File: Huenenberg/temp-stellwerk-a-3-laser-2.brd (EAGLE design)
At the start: 99.1 x 61 mm, 120 parts, among them Q1 BSS123, Q10 BSS84, Q11 BSS123, Q12 BSS84, Q13 BSS123, Q14 BSS84, Q15 BSS123, Q16 BSS84, Q17 BSS123, Q18 BSS84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

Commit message: Adds circles to laser around the tactile buttons.
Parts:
- H1, H2, H3: value MOUNT-HOLE3.2 -> MOUNT-HOLE4.0-LASER; device holes:3,2 -> eagleparts:MOUNT-HOLE-3.2-4.0-LASER
- LOCK, W1, W1011, W34, W56, W89: device g-e2e-training:TACTSW-6X6 -> eagleparts:TACTSW-6X6-LASER
- TRK1, TRK2, TRK3, TRK4, TRK5, TRK6, W2A, W2B, W7A, W7B: value (none) -> TACTSW-6X6S; device g-e2e-training:TACTSW-6X6 -> eagleparts:TACTSW-6X6-LASER

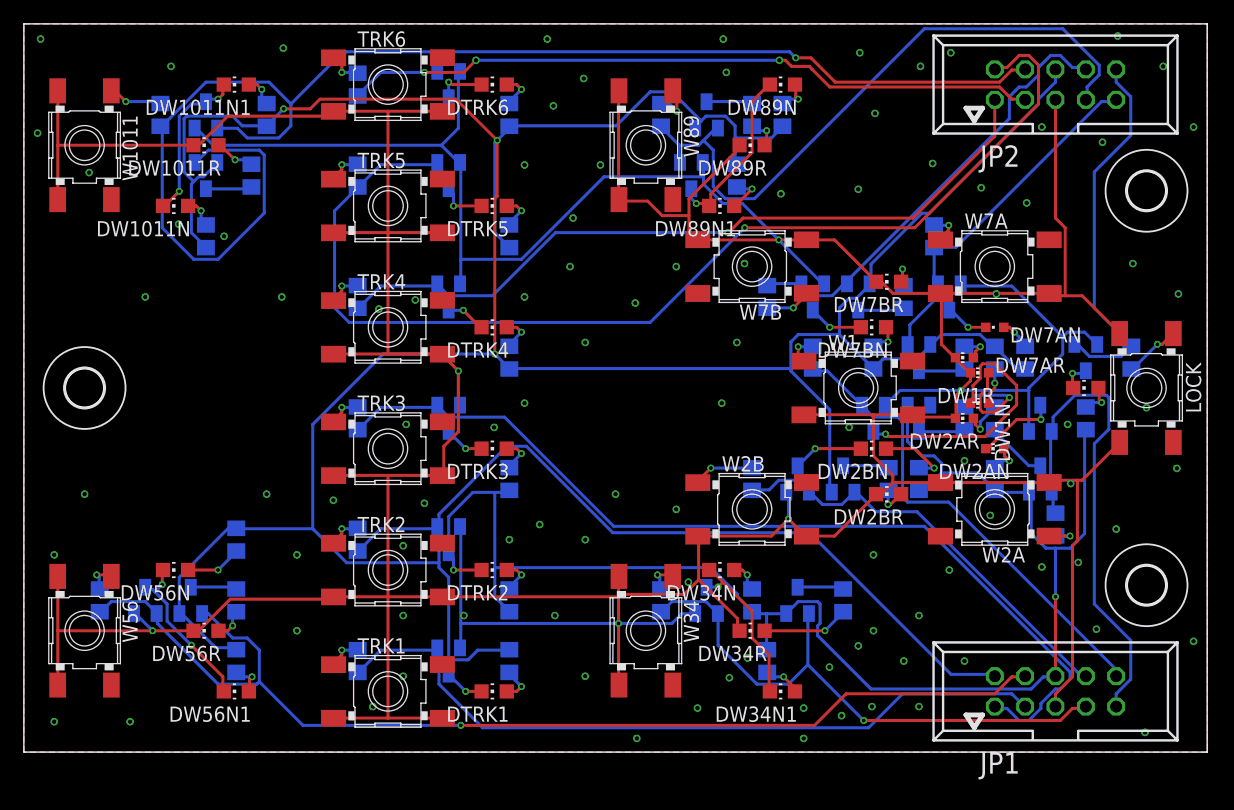
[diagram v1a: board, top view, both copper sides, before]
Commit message: Adds laser holes on top of the LEDs.
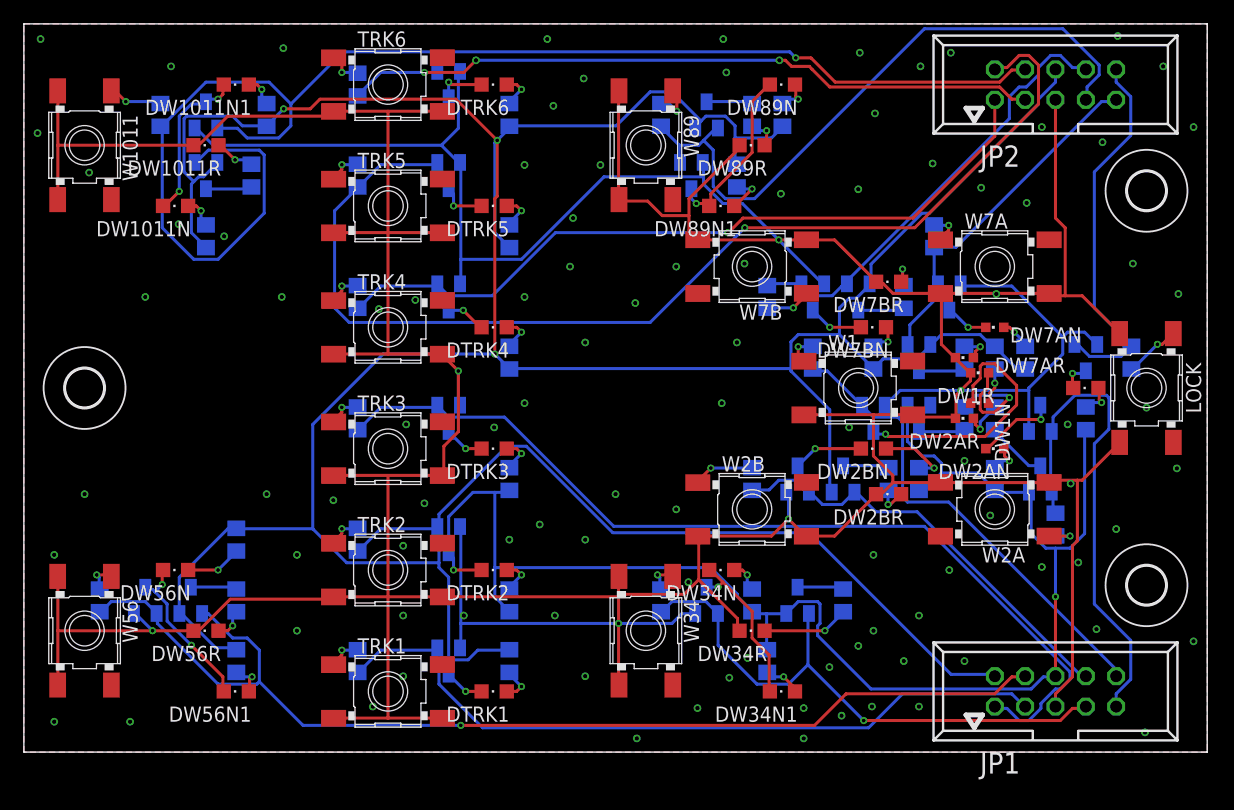
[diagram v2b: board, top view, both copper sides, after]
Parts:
- DLOCK, DTRK1, DTRK2, DTRK3, DTRK4, DTRK5, DTRK6, DW1011N, DW1011N1, DW1011R, DW2BN, DW2BR, DW34N, DW34N1, DW34R, DW56N, DW56N1, DW56R, DW7BN, DW7BR, DW89N, DW89N1, DW89R: device led:CHIP-LED0805 -> eagleparts:CHIPLED_0805
- DW1N, DW1R, DW2AN, DW2AR, DW7AR: device led:CHIP-LED0603 -> eagleparts:CHIPLED_0603
